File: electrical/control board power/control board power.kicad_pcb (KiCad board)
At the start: 2 copper layers, 72.4 x 149.8 mm, 39 parts, among them J1 48V_IN, J2 5V, J4 Conn_01x08, J5 Conn_01x05, J6 Power_Connector, U1 LD1117S33TR_SOT223, U2 LTC7103-LT7103, U3 LTC7103-LT7103, U4 INA240-INA240

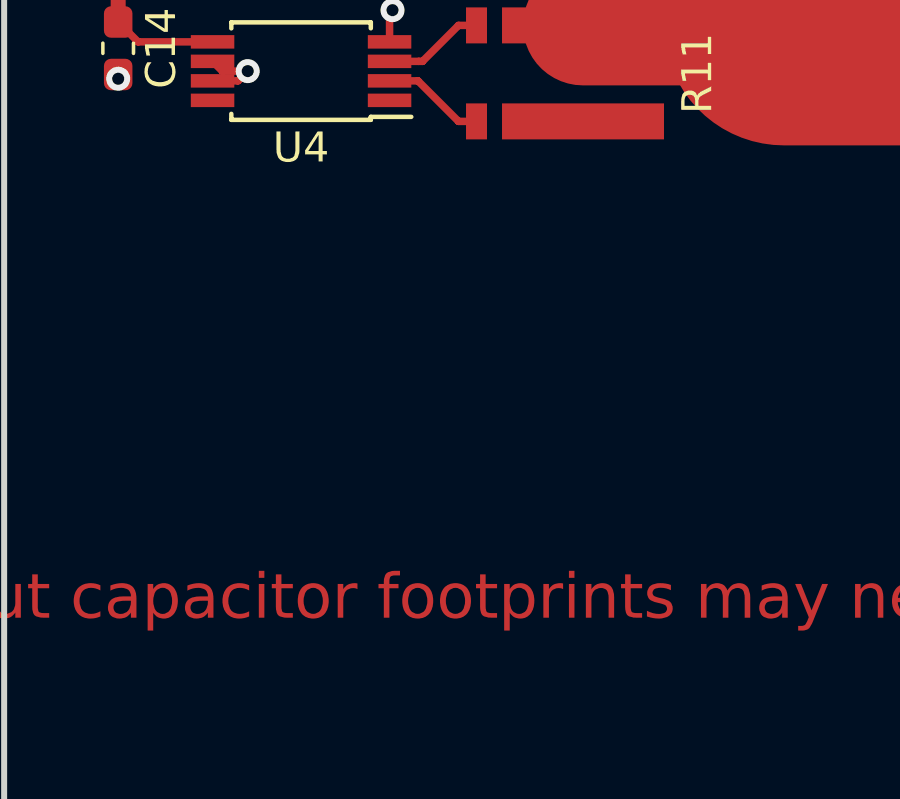
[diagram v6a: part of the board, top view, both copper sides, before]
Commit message: found a part for the barrel jack
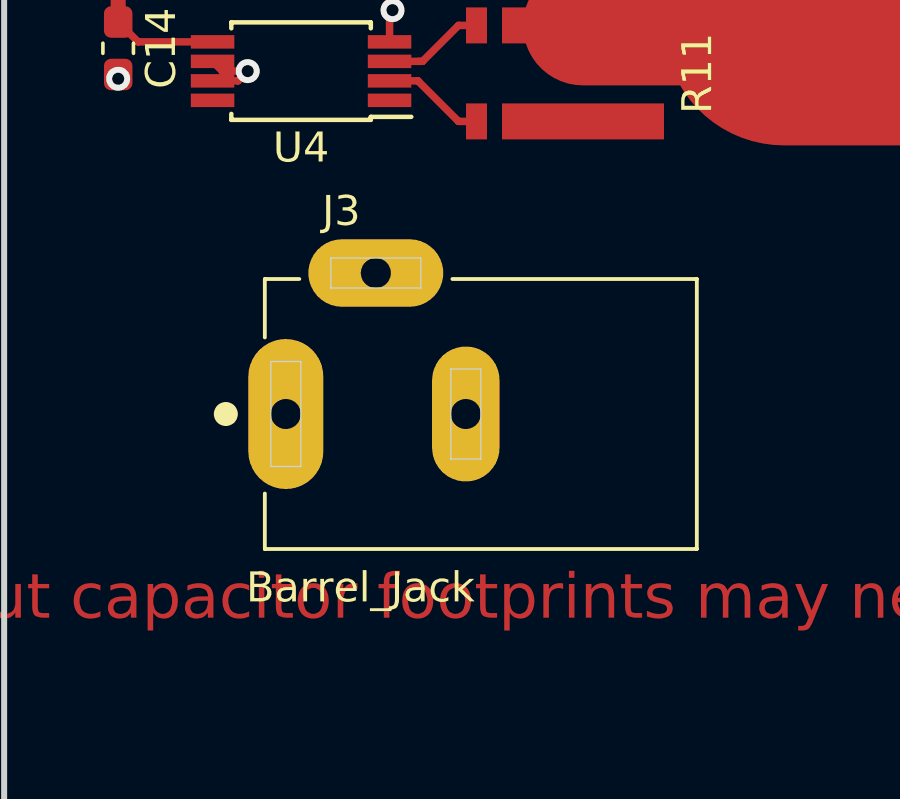
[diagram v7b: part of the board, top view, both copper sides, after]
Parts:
- added J3: Barrel_Jack, PJ-002AH:CUI_PJ-002AH, F.Cu at (98.3, 153.2)
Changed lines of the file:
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@@
     (tracks 325)
     (zones 0)
-    (modules 39)
+    (modules 40)
     (nets 45)
   )
@@
       (net 17 /48V_IN))
   )
+  (module PJ-002AH:CUI_PJ-002AH (layer F.Cu)
+    (at 98.298 153.162)
+    (fp_text reference J3 (at 1.85009 -6.76532) (layer F.SilkS)
+      (effects (font (size 1.00005 1.00005) (thickness 0.05)))
+    )
+    (fp_text value Barrel_Jack (at 2.48828 5.78266) (layer F.SilkS)
+      (effects (font (size 1.00132 1.00132) (thickness 0.05)))
+    )
+    (fp_line (start 0.5 1.75) (end -0.5 1.75) (layer Edge.Cuts) (width 0.0001))
+    (fp_line (start -0.5 1.75) (end -0.5 -1.75) (layer Edge.Cuts) (width 0.0001))
+    (fp_line (start -0.5 -1.75) (end 0.5 -1.75) (layer Edge.Cuts) (width 0.0001))
+    (fp_line (start 0.5 -1.75) (end 0.5 1.75) (layer Edge.Cuts) (width 0.0001))
+    (fp_line (start 6.5 1.5) (end 5.5 1.5) (layer Edge.Cuts) (width 0.0001))
+    (fp_line (start 5.5 1.5) (end 5.5 -1.5) (layer Edge.Cuts) (width 0.0001))
+    (fp_line (start 5.5 -1.5) (end 6.5 -1.5) (layer Edge.Cuts) (width 0.0001))
+    (fp_line (start 6.5 -1.5) (end 6.5 1.5) (layer Edge.Cuts) (width 0.0001))
+    (fp_line (start 1.5 -4.2) (end 1.5 -5.2) (layer Edge.Cuts) (width 0.0001))
+    (fp_line (start 1.5 -5.2) (end 4.5 -5.2) (layer Edge.Cuts) (width 0.0001))
+    (fp_line (start 4.5 -5.2) (end 4.5 -4.2) (layer Edge.Cuts) (width 0.0001))
+    (fp_line (start 4.5 -4.2) (end 1.5 -4.2) (layer Edge.Cuts) (width 0.0001))
+    (fp_line (start -0.7 -4.5) (end 13.7 -4.5) (layer Dwgs.User) (width 0.127))
+    (fp_line (start 13.7 -4.5) (end 13.7 4.5) (layer Dwgs.User) (width 0.127))
+    (fp_line (start 13.7 4.5) (end -0.7 4.5) (layer Dwgs.User) (width 0.127))
+    (fp_line (start -0.7 4.5) (end -0.7 -4.5) (layer Dwgs.User) (width 0.127))
+    (fp_line (start 13.7 -4.5) (end 13.7 4.5) (layer F.SilkS) (width 0.127))
+    (fp_line (start 13.7 4.5) (end -0.7 4.5) (layer F.SilkS) (width 0.127))
+    (fp_line (start -0.7 -4.5) (end 0.45 -4.5) (layer F.SilkS) (width 0.127))
+    (fp_line (start -0.7 4.5) (end -0.7 2.65) (layer F.SilkS) (width 0.127))
+    (fp_line (start 5.55 -4.5) (end 13.7 -4.5) (layer F.SilkS) (width 0.127))
+    (fp_line (start -0.7 -2.55) (end -0.7 -4.5) (layer F.SilkS) (width 0.127))
+    (fp_line (start -1 -4.75) (end 0.45 -4.75) (layer Eco1.User) (width 0.05))
+    (fp_line (start 0.45 -4.75) (end 0.45 -6.1) (layer Eco1.User) (width 0.05))
+    (fp_line (start 0.45 -6.1) (end 5.55 -6.1) (layer Eco1.User) (width 0.05))
+    (fp_line (start 5.55 -6.1) (end 5.55 -4.75) (layer Eco1.User) (width 0.05))
+    (fp_line (start 5.55 -4.75) (end 14 -4.75) (layer Eco1.User) (width 0.05))
+    (fp_line (start 14 -4.75) (end 14 4.75) (layer Eco1.User) (width 0.05))
+    (fp_line (start 14 4.75) (end -1 4.75) (layer Eco1.User) (width 0.05))
+    (fp_line (start -1 4.75) (end -1 2.35) (layer Eco1.User) (width 0.05))
+    (fp_circle (center -2 0) (end -1.8 0) (layer F.SilkS) (width 0.4))
+    (fp_line (start -1 -2.25) (end -1 -4.75) (layer Eco1.User) (width 0.05))
+    (fp_line (start -1 -2.25) (end -1.55 -2.25) (layer Eco1.User) (width 0.05))
+    (fp_line (start -1.55 -2.25) (end -1.55 2.35) (layer Eco1.User) (width 0.05))
+    (fp_line (start -1.55 2.35) (end -1 2.35) (layer Eco1.User) (width 0.05))
+    (pad 1 thru_hole oval (at 0 0 90) (size 5 2.5) (drill 1) (layers *.Cu *.Mask)
+      (net 4 +12V))
+    (pad 2 thru_hole oval (at 6 0 90) (size 4.5 2.25) (drill 1) (layers *.Cu *.Mask)
+      (net 1 GND))
+    (pad 3 thru_hole oval (at 3 -4.7 180) (size 4.5 2.25) (drill 1) (layers *.Cu *.Mask))
+  )
   (gr_text "input capacitor footprints may need to be changed if capacitors don't have the proper voltage rating" (at 137.16 159.258) (layer F.Cu)

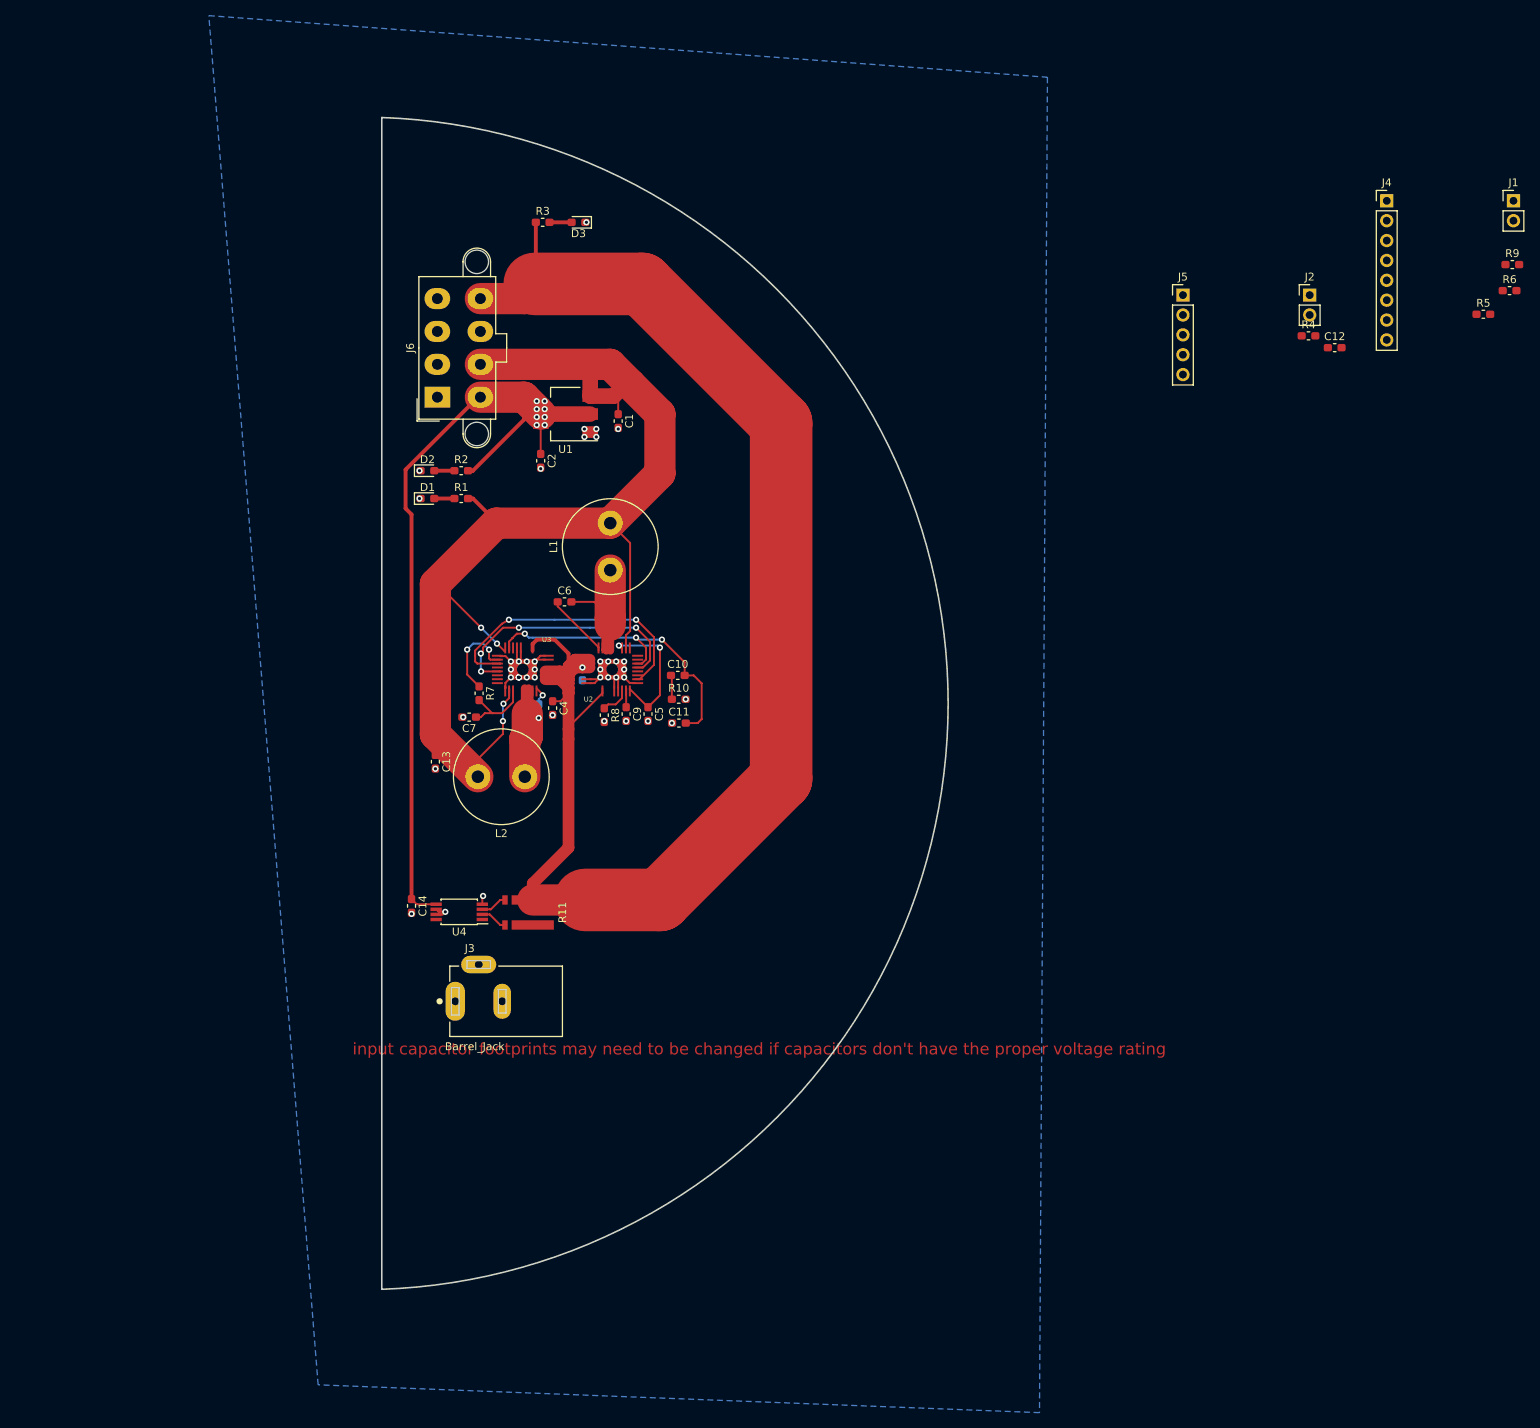
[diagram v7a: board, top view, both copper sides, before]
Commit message: found parts for most of the stuff on the control board
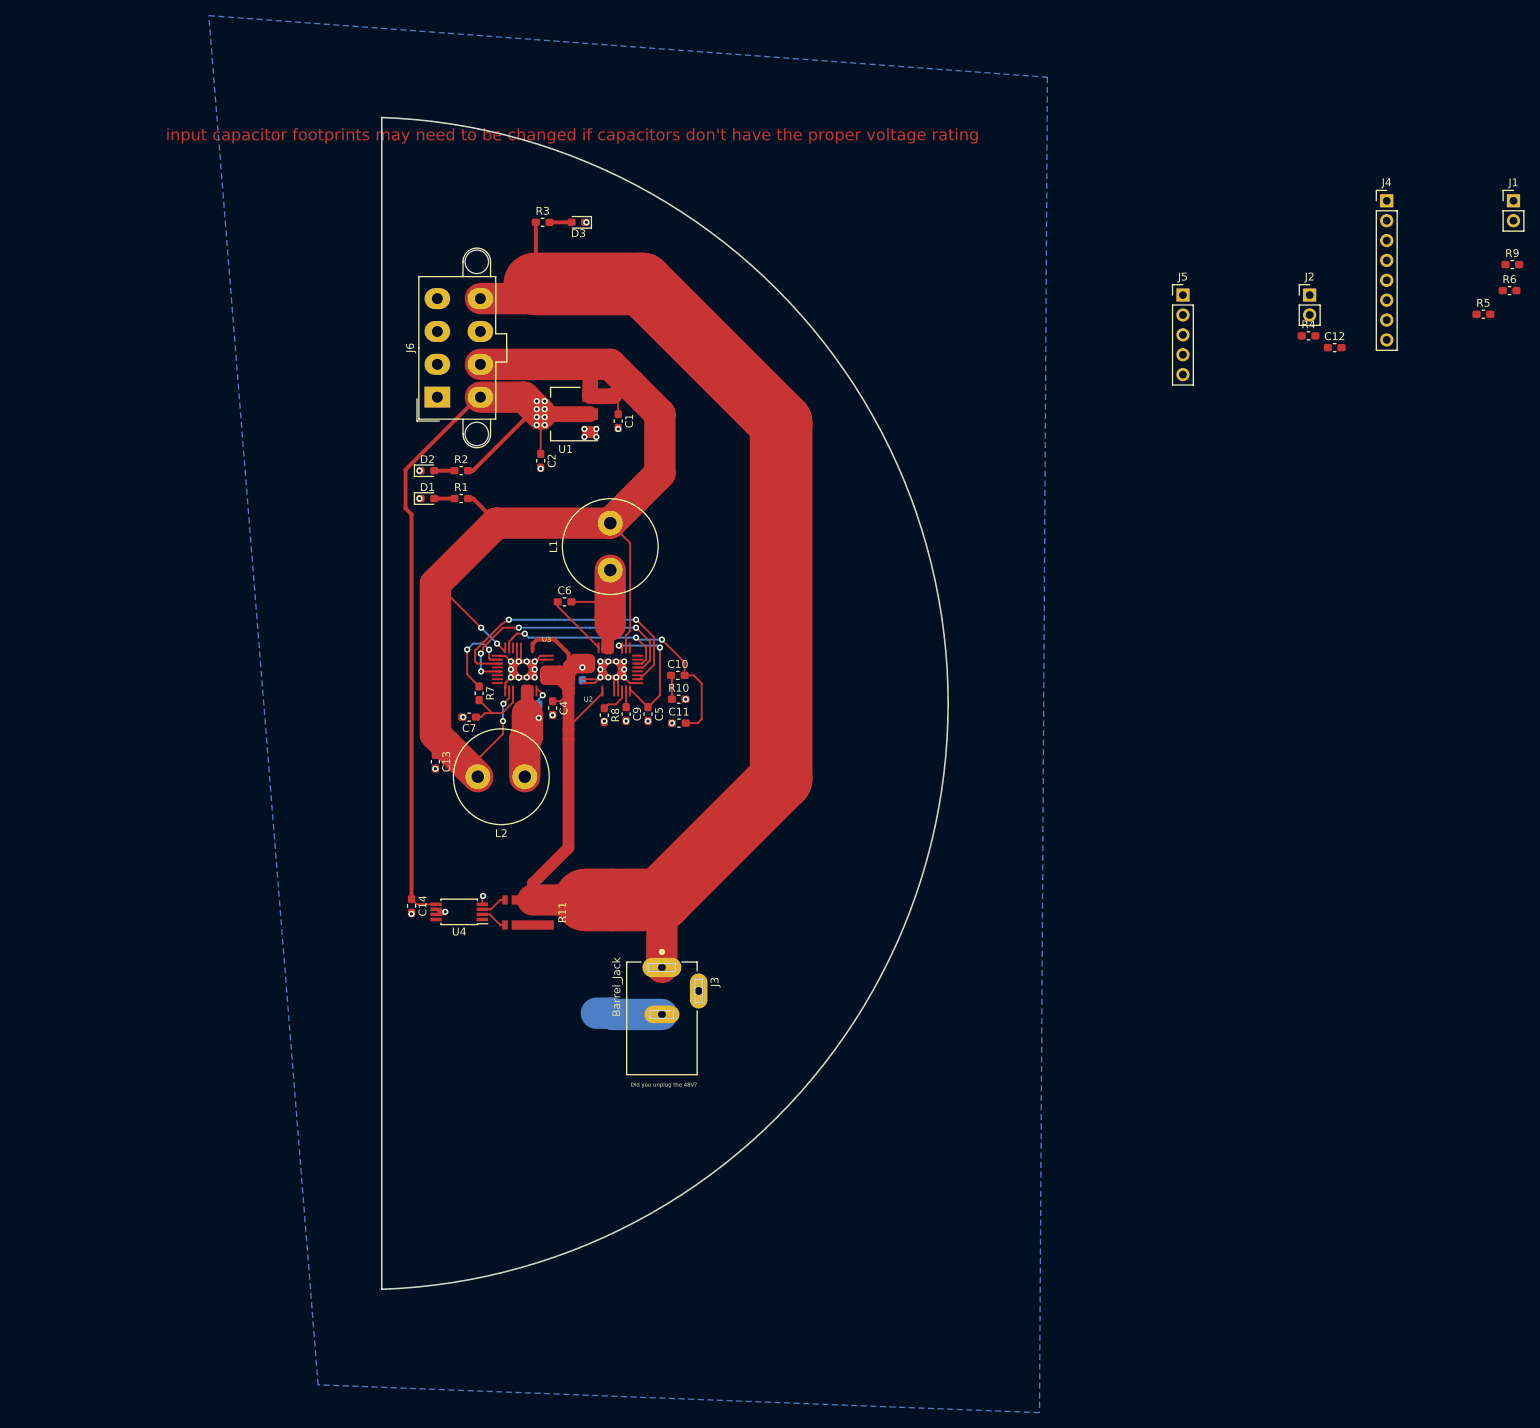
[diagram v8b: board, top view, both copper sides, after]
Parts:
- moved J3 26.8 mm to (124.7, 148.8), turned to 270 degrees
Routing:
- net +12V: track 212.2 -> 220.9 mm
- net GND: track 22.9 -> 31.4 mm
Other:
- board text added: "Did you unplug the 48V?"
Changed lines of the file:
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@@
   (general
     (thickness 1.6)
-    (drawings 3)
-    (tracks 325)
+    (drawings 4)
+    (tracks 331)
     (zones 0)
     (modules 40)
@@
   )
   (module PJ-002AH:CUI_PJ-002AH (layer F.Cu)
-    (at 98.298 153.162)
-    (fp_text reference J3 (at 1.85009 -6.76532) (layer F.SilkS)
+    (at 124.714 148.844 270)
+    (fp_text reference J3 (at 1.85009 -6.76532 270) (layer F.SilkS)
       (effects (font (size 1.00005 1.00005) (thickness 0.05)))
     )
-    (fp_text value Barrel_Jack (at 2.48828 5.78266) (layer F.SilkS)
+    (fp_text value Barrel_Jack (at 2.48828 5.78266 270) (layer F.SilkS)
       (effects (font (size 1.00132 1.00132) (thickness 0.05)))
     )
@@
     (fp_line (start -1.55 -2.25) (end -1.55 2.35) (layer Eco1.User) (width 0.05))
     (fp_line (start -1.55 2.35) (end -1 2.35) (layer Eco1.User) (width 0.05))
-    (pad 1 thru_hole oval (at 0 0 90) (size 5 2.5) (drill 1) (layers *.Cu *.Mask)
+    (pad 1 thru_hole oval (at 0 0) (size 5 2.5) (drill 1) (layers *.Cu *.Mask)
       (net 4 +12V))
-    (pad 2 thru_hole oval (at 6 0 90) (size 4.5 2.25) (drill 1) (layers *.Cu *.Mask)
-      (net 1 GND))
-    (pad 3 thru_hole oval (at 3 -4.7 180) (size 4.5 2.25) (drill 1) (layers *.Cu *.Mask))
-  )
-  (gr_text "input capacitor footprints may need to be changed if capacitors don't have the proper voltage rating" (at 137.16 159.258) (layer F.Cu)
+    (pad 2 thru_hole oval (at 6 0) (size 4.5 2.25) (drill 1) (layers *.Cu *.Mask)
+      (net 1 GND))
+    (pad 3 thru_hole oval (at 3 -4.7 90) (size 4.5 2.25) (drill 1) (layers *.Cu *.Mask))
+  )
+  (gr_text "Did you unplug the 48V?" (at 124.968 163.83) (layer F.SilkS)
+    (effects (font (size 0.5 0.5) (thickness 0.125)))
+  )
+  (gr_text "input capacitor footprints may need to be changed if capacitors don't have the proper voltage rating" (at 113.284 42.418) (layer F.Cu)
     (effects (font (size 1.5 1.5) (thickness 0.3)))
   )
@@
   (segment (start 101.756 139.798) (end 101.854 139.7) (width 0.25) (layer F.Cu) (net 1))
   (segment (start 101.756 140.757) (end 101.756 139.798) (width 0.25) (layer F.Cu) (net 1))
+  (segment (start 118.464 154.844) (end 118.306 154.686) (width 4) (layer B.Cu) (net 1))
+  (segment (start 124.714 154.844) (end 118.464 154.844) (width 4) (layer B.Cu) (net 1))
+  (segment (start 118.306 154.686) (end 116.332 154.686) (width 4) (layer B.Cu) (net 1))
   (segment (start 105.184 113.744) (end 105.184 113.144) (width 0.25) (layer F.Cu) (net 2) (status 30))
   (segment (start 118.11 92.044) (end 120.65 94.584) (width 0.25) (layer F.Cu) (net 2) (status 10))
@@
   (segment (start 112.776 133.536) (end 112.776 119.634) (width 1.5) (layer F.Cu) (net 4))
   (segment (start 108.204 140.208) (end 114.904 140.208) (width 4) (layer F.Cu) (net 4))
-  (segment (start 114.904 140.208) (end 124.46 140.208) (width 8) (layer F.Cu) (net 4))
   (segment (start 124.46 140.208) (end 139.954 124.714) (width 8) (layer F.Cu) (net 4))
   (segment (start 139.954 124.714) (end 139.954 79.248) (width 8) (layer F.Cu) (net 4))
@@
   (segment (start 108.599 61.327) (end 108.458 61.468) (width 0.5) (layer F.Cu) (net 4))
   (segment (start 108.599 53.594) (end 108.599 61.327) (width 0.5) (layer F.Cu) (net 4))
+  (segment (start 114.904 140.208) (end 118.364 140.208) (width 8) (layer F.Cu) (net 4))
+  (segment (start 118.364 140.208) (end 124.46 140.208) (width 8) (layer F.Cu) (net 4))
+  (segment (start 124.714 140.462) (end 124.46 140.208) (width 4) (layer F.Cu) (net 4))
+  (segment (start 124.714 148.844) (end 124.714 140.462) (width 4) (layer F.Cu) (net 4))
   (segment (start 120.614 113.248) (end 120.614 113.144) (width 0.25) (layer F.Cu) (net 5))
   (segment (start 122.936 115.57) (end 120.614 113.248) (width 0.25) (layer F.Cu) (net 5))
